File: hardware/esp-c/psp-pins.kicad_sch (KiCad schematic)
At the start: 29 parts, among them U10 HC-FPC-05-09-10RLTAG, U11 HC-FPC-05-09-10RLTAG, U13 AFC42-S14FMA-1H, U5 MCP42010T-I/SL, U6 HC-FPC-05-09-10RLTAG, U7 IPFP051A30472R5

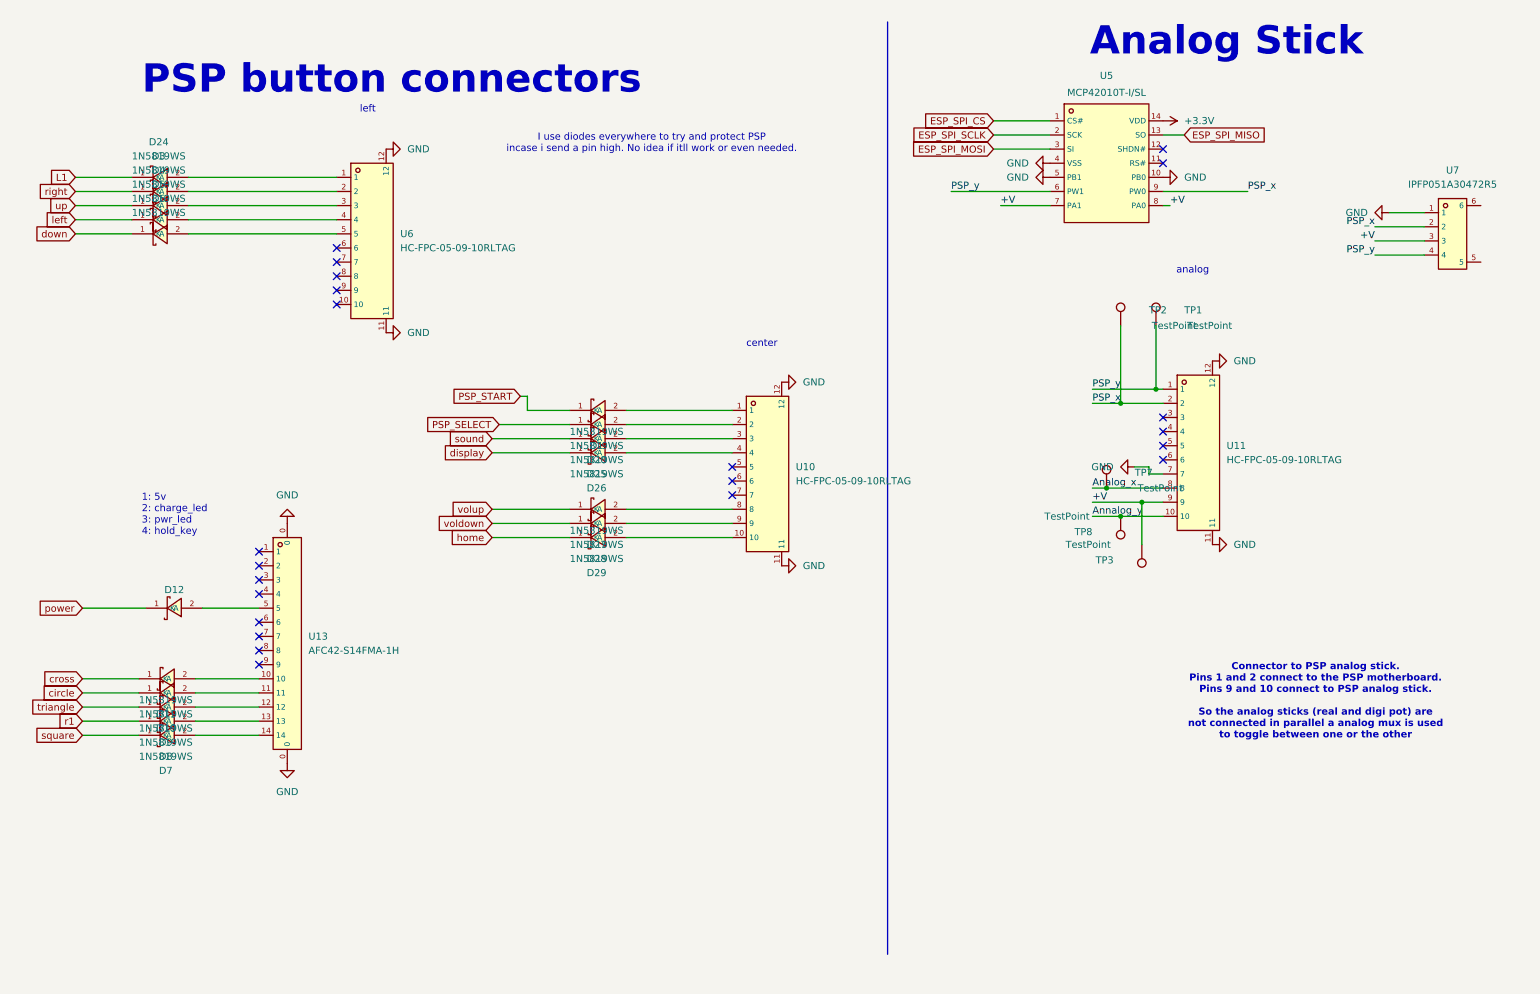
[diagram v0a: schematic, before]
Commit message: Cleaned up psp pins schematic sheet and added backups and lock files to gitignore file.
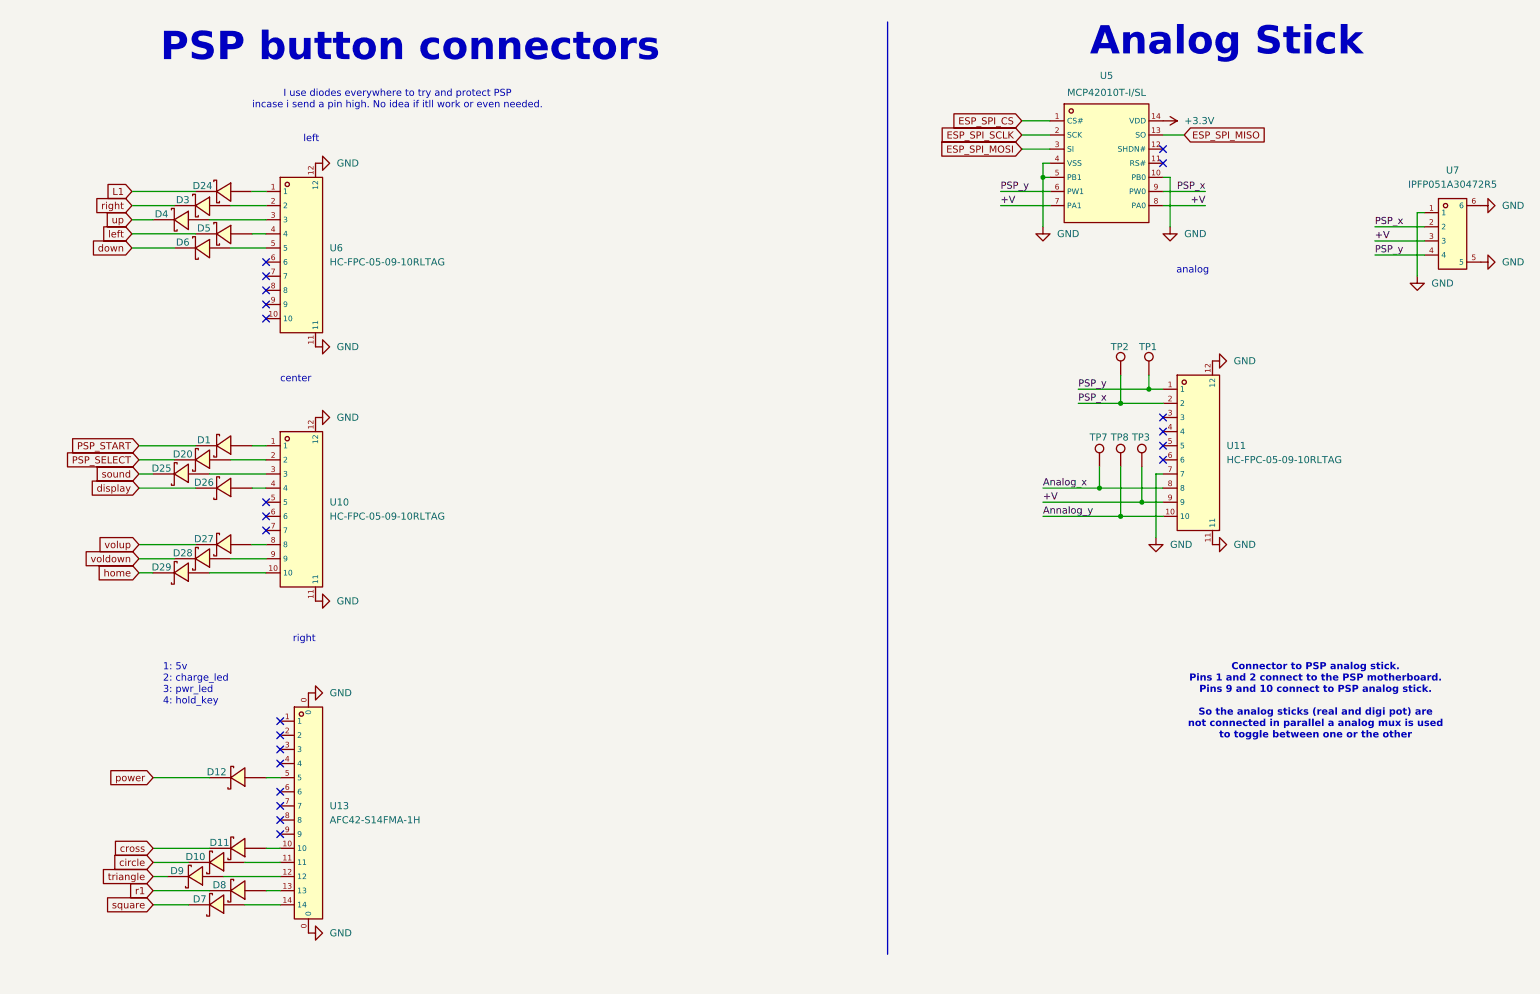
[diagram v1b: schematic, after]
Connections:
- net GND: now also U7.5, U7.6
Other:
- note added: "right"
- moved on the sheet: TP1, TP2, TP3, TP7, TP8, U10, U13, U6

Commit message: Add right-hand board connector, restructure schematic sheet for button connectors.
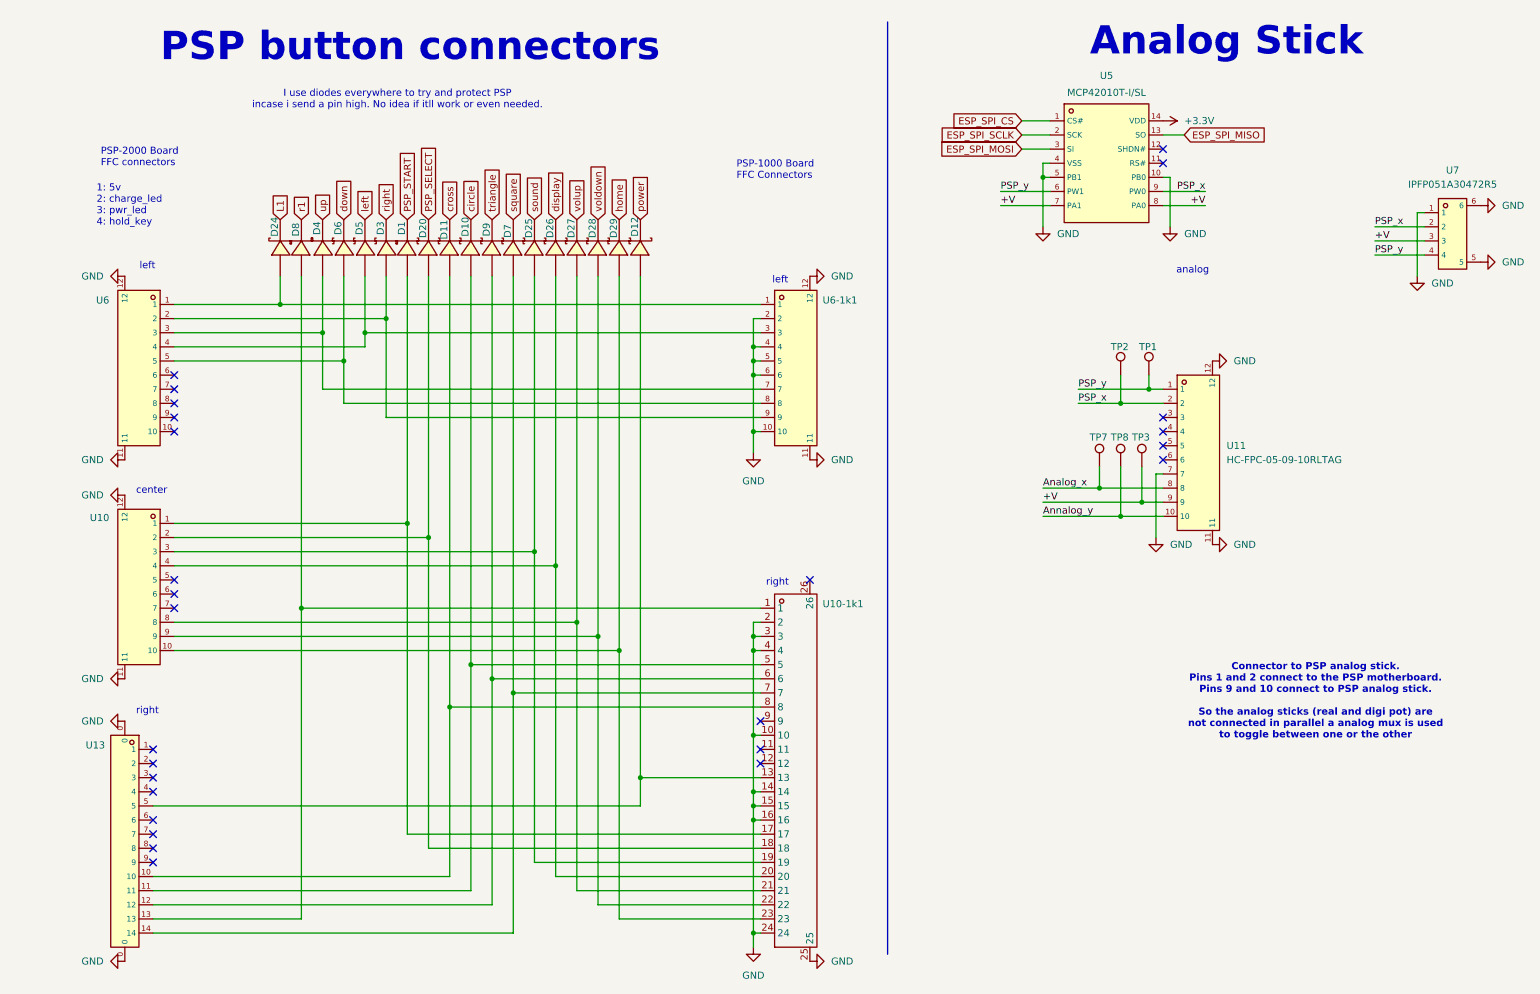
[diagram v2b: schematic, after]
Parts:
- added U10-1k1: ~, JLCPCB_footprint:FPC-SMD_24P-P0.50_HC-FPC-05-09-24RLTAG, symbol JLCPCB_schematic:HC-FPC-05-09-24RLTAG
- added U6-1k1: HC-FPC-05-09-10RLTAG, JLCPCB_footprint:FPC-SMD_10P-P0.50_HC-FPC-05-09-10RLTAG, symbol JLCPCB_schematic:HC-FPC-05-09-10RLTAG
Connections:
- net GND: now also U10-1k1.10, U10-1k1.14, U10-1k1.15, U10-1k1.16, U10-1k1.2, U10-1k1.24, U10-1k1.25, U10-1k1.3, U10-1k1.4, U6-1k1.10, U6-1k1.11, U6-1k1.12, U6-1k1.2, U6-1k1.4, U6-1k1.5, U6-1k1.6
- net at D5.2 (A), U6.4: now also U6-1k1.3
- net at D7.2 (A), U13.14: now also U10-1k1.7
- net at D10.2 (A), U13.11: now also U10-1k1.5
- net at D24.2 (A), U6.1: now also U6-1k1.1
- net at D3.2 (A), U6.2: now also U6-1k1.9
- net at D4.2 (A), U6.3: now also U6-1k1.7
- net at D6.2 (A), U6.5: now also U6-1k1.8
- net at D1.2 (A), U10.1: now also U10-1k1.17
- net at D29.2 (A), U10.10: now also U10-1k1.23
- net at D20.2 (A), U10.2: now also U10-1k1.18
- net at D25.2 (A), U10.3: now also U10-1k1.19
- net at D26.2 (A), U10.4: now also U10-1k1.20
- net at D27.2 (A), U10.8: now also U10-1k1.21
- net at D28.2 (A), U10.9: now also U10-1k1.22
- net at D11.2 (A), U13.10: now also U10-1k1.8
- net at D9.2 (A), U13.12: now also U10-1k1.6
- net at D8.2 (A), U13.13: now also U10-1k1.1
- net at D12.2 (A), U13.5: now also U10-1k1.13
- no-connect marks 22 -> 26
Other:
- note added: "PSP-1000 Board FFC Connectors"
- note added: "PSP-2000 Board FFC connectors"
- moved on the sheet: D1, D10, D11, D12, D20, D24, D25, D26, D27, D28, D29, D3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
